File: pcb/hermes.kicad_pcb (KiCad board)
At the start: 2 copper layers, 90 x 33.5 mm, 12 parts, among them J1 OLED_128x64, U1 XIAO-RP2040-DIP, U2 MAX30102

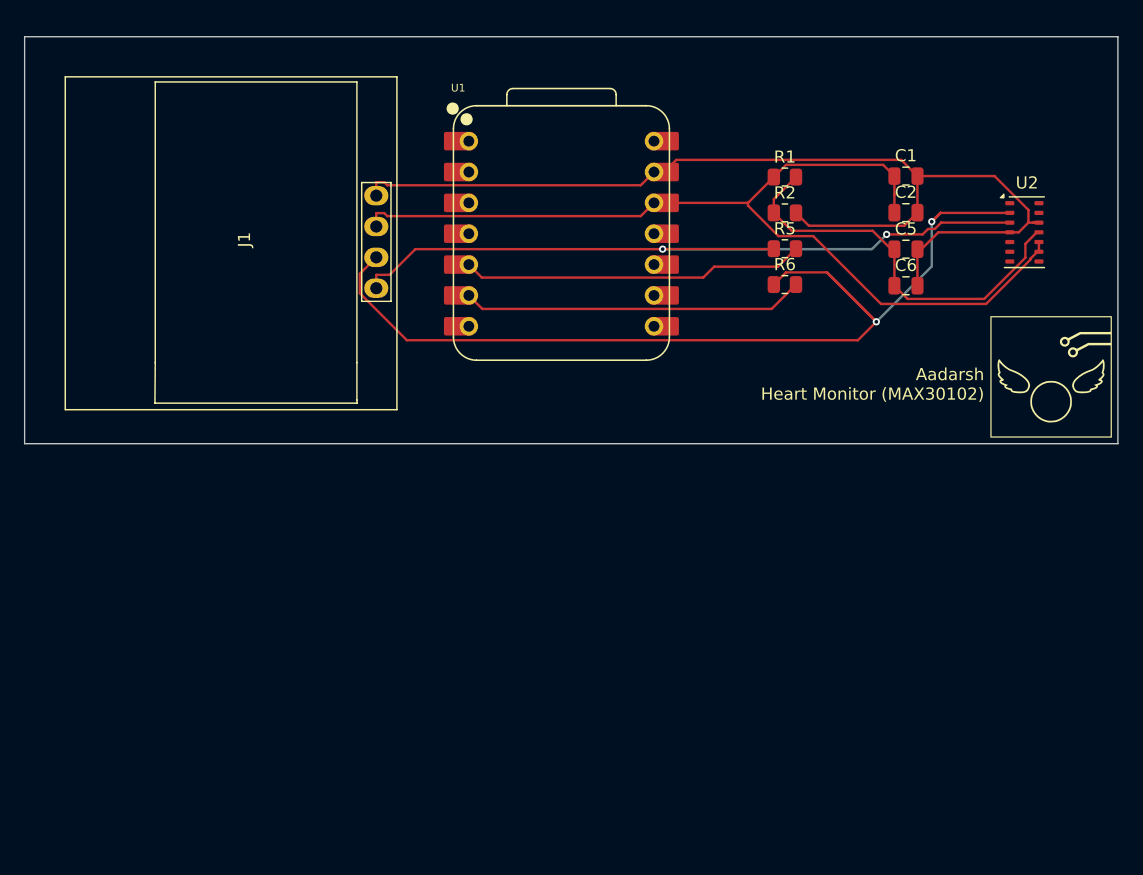
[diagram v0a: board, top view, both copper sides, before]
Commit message: reroute board to incorporate TOF sensor
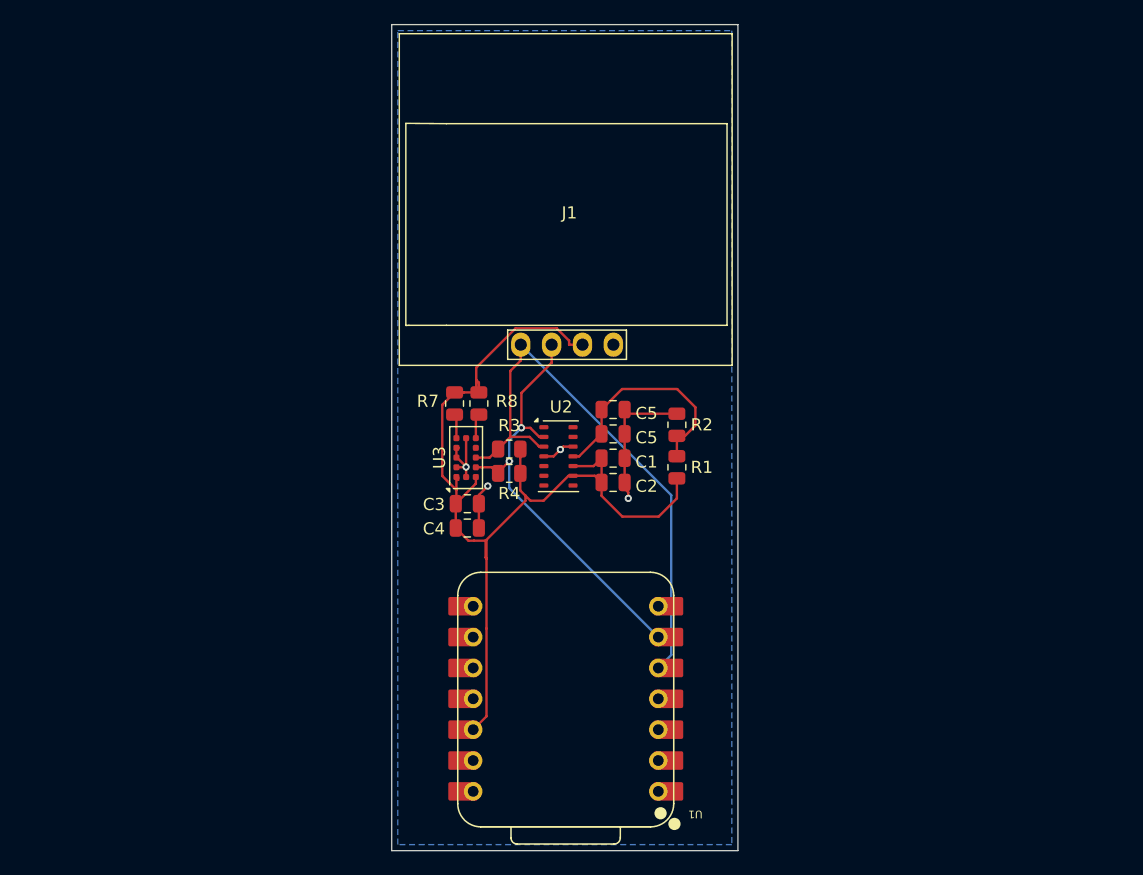
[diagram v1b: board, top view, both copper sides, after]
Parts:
- removed R5, R6: 4.7k, Resistor_SMD:R_0805_2012Metric
- added C3: 100nF, Capacitor_SMD:C_0805_2012Metric, F.Cu at (138.4, 105.4)
- added C4: 4.7uF, Capacitor_SMD:C_0805_2012Metric, F.Cu at (138.4, 107.4)
- added R3: 5.1k, Resistor_SMD:R_0805_2012Metric, F.Cu at (141.9, 100.9)
- added R4: 5.1k, Resistor_SMD:R_0805_2012Metric, F.Cu at (141.9, 102.9)
- added R7: 5.1k, Resistor_SMD:R_0805_2012Metric, F.Cu at (137.4, 97.2)
- added R8: 5.1k, Resistor_SMD:R_0805_2012Metric, F.Cu at (139.4, 97.2)
- added U3: VL53L1CXV0FY1, Sensor_Distance:ST_VL53L1x, F.Cu at (138.3, 101.6)
- G***: moved to B.Cu
- R1: value 80 -> 1k
- R2: value 80 -> 2.2k
- moved G*** 56.2 mm to (191.5, 39.0), turned to 90 degrees
- moved U2 42.6 mm to (145.9, 101.5)
- moved U1 38.3 mm to (146.5, 121.5), turned to 180 degrees
- moved C1 33.5 mm to (150.4, 101.7)
- moved C2 32.8 mm to (150.4, 103.7)
- moved C5 27.5 mm to (150.4, 97.7)
- moved C6 27.0 mm to (150.4, 99.7)
- moved J1 26.6 mm to (146.8, 81.8), turned to 180 degrees
- moved R1 25.5 mm to (155.7, 102.4), turned to 90 degrees
- moved R2 19.6 mm to (155.7, 98.9), turned to 90 degrees
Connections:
- U1 pad 5: Net-(U1-GPIO6/SDA) -> SDA
- U1 pad 6: Net-(U1-GPIO7/SCL) -> SCL
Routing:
- net SCL: track 102.8 -> 37.3 mm
- net GND: track 86.3 -> 25.3 mm, vias 0 -> 4
- net Net-(U1-GPIO6/SDA): track 29.2 -> 0.00 mm
- net Net-(U1-GPIO7/SCL): track 29.1 -> 0.00 mm
- net SDA: track 64.2 -> 47.6 mm, vias 2 -> 0
- net +1V8: track 33.2 -> 19.4 mm
- net +3V3: track 79.1 -> 86.0 mm
- net TOF_INT: track 0.00 -> 2.04 mm
- net XSHUT: track 0.00 -> 2.00 mm
- added copper zone on B.Cu, net GND
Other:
- board size 90 x 33.5 mm -> 28.5 x 68 mm
- board text added: "Aadarsh Heart Monitor (MAX30102) TOF Sensor (VL53L1X)"
- board text added: "C5"
- board text removed: "Aadarsh Heart Monitor (MAX30102)"
